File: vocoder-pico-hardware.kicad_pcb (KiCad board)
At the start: 2 copper layers, 57 x 108 mm, 68 parts, among them J1 Conn_02x05_Odd_Even, J2 AudioJack2_SwitchT, J3 AudioJack2_SwitchT, Q1 BC547, Q2 BC547, Q3 BC547, Q4 BC547, SW1 SW_Push, SW2 SW_Push, U1 TL072, U2 LM7805_TO220, U3 PCM5100A, U4 SC39-11GWA, U5 SC39-11GWA, U6 SC39-11GWA, U7 SC39-11GWA, U8 MCP6002-xP

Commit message: re-route D3
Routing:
- net +5V: track 20.1 -> 107.5 mm
- net Vsys: track 0.00 -> 20.8 mm

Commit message: add vdd on potentiometers
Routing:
- net Vdd: track 163.3 -> 205.8 mm, vias 0 -> 1
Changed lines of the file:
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@@
+	)
+	(segment
+		(start 58.559 59.659)
+		(end 73.721 59.659)
+		(width 0.5)
+		(layer "F.Cu")
+		(net 20)
 	)
 	(segment
@@
 	)
 	(segment
+		(start 81.279 62.199)
+		(end 81.279 60.421108)
+		(width 0.5)
+		(layer "F.Cu")
+		(net 20)
+	)
+	(segment
 		(start 80.3625 75.075)
 		(end 77.425 75.075)
@@
 	)
 	(segment
+		(start 81.279 60.421108)
+		(end 82.041108 59.659)
+		(width 0.5)
+		(layer "F.Cu")
+		(net 20)
+	)
+	(segment
 		(start 70.485 73.98)
 		(end 70.485 71.815)
@@
 	)
 	(segment
+		(start 82.041108 59.659)
+		(end 83.158999 59.659)
+		(width 0.5)
+		(layer "F.Cu")
+		(net 20)
+	)
+	(segment
 		(start 77.243182 110.743182)
 		(end 77.5 111)
@@
 	)
 	(segment
+		(start 82.58 63.5)
+		(end 81.279 62.199)
+		(width 0.5)
+		(layer "F.Cu")
+		(net 20)
+	)
+	(segment
 		(start 80.3625 74.1375)
 		(end 80.3625 75.025)
@@
 	)
 	(segment
+		(start 83.158999 59.659)
+		(end 84.968962 61.468963)
+		(width 0.5)
+		(layer "F.Cu")
+		(net 20)
+	)
+	(segment
+		(start 73.721 59.659)
+		(end 75.5 61.438)
+		(width 0.5)
+		(layer "F.Cu")
+		(net 20)
+	)
+	(segment
 		(start 80.3625 77.025)
 		(end 81.475 77.025)
@@
 	)
 	(segment
+		(start 75.5 61.438)
+		(end 75.5 66)
+		(width 0.5)
+		(layer "F.Cu")
+		(net 20)
+	)
+	(segment
 		(start 67.354 98.043182)
 		(end 67.354 81.598)
@@
 	)
 	(segment
+		(start 56.9 58)
+		(end 58.559 59.659)
+		(width 0.5)
+		(layer "F.Cu")
+		(net 20)
+	)
+	(segment
 		(start 76.625 79.625)
 		(end 77.25 79)
@@
 		(net 20)
 	)
+	(via
+		(at 84.968962 61.468963)
+		(size 0.6)
+		(drill 0.3)
+		(layers "F.Cu" "B.Cu")
+		(net 20)
+	)
+	(segment
+		(start 89.631037 61.468963)
+		(end 93.1 58)
+		(width 0.5)
+		(layer "B.Cu")
+		(net 20)
+	)
+	(segment
+		(start 84.968962 61.468963)
+		(end 89.631037 61.468963)
+		(width 0.5)
+		(layer "B.Cu")
+		(net 20)
+	)

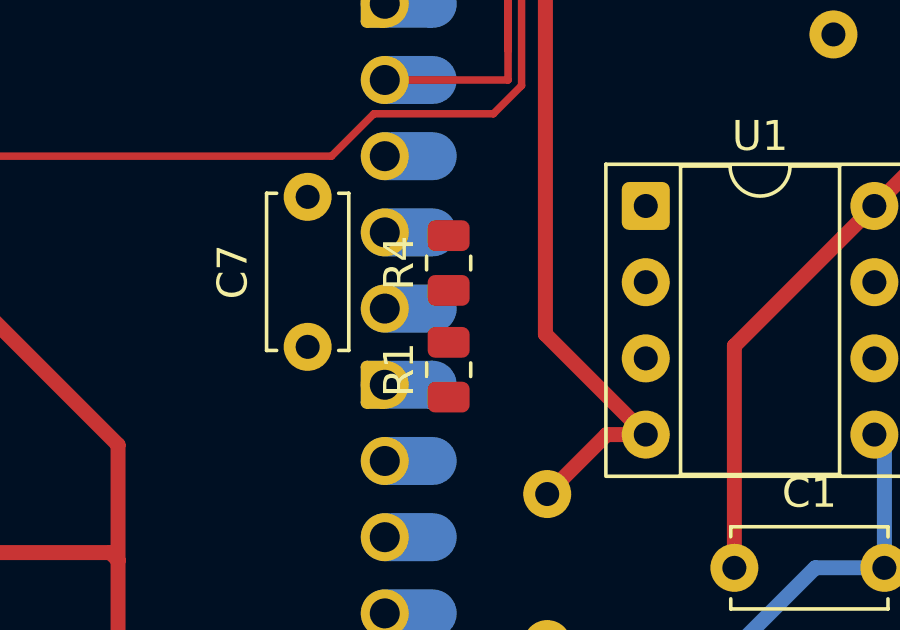
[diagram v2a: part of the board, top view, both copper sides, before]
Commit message: repossitioning smd resistors
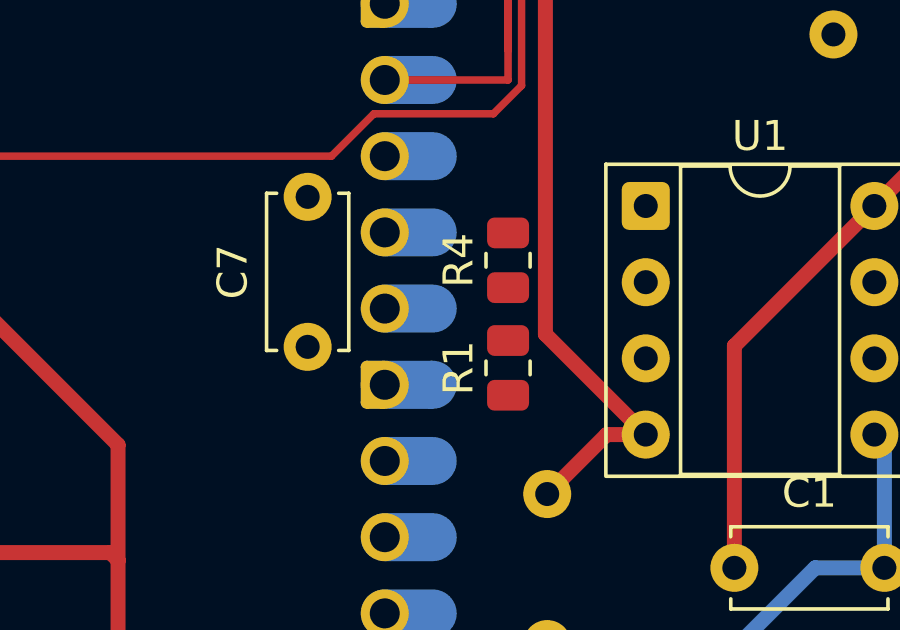
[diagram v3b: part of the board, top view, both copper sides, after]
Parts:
- moved R4 1.98 mm to (90.5, 101.0)
- moved R1 1.98 mm to (90.5, 104.6)
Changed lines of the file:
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@@
 	(footprint "Resistor_SMD:R_0805_2012Metric"
 		(layer "F.Cu")
-		(at 88.519 101.092 90)
+		(at 90.5 101 90)
 		(descr "Resistor SMD 0805 (2012 Metric), square (rectangular) end terminal, IPC-7351 nominal, (Body size source: IPC-SM-782 page 72, https://www.pcb-3d.com/wordpress/wp-content/uploads/ipc-sm-782a_amendment_1_and_2.pdf), generated with kicad-footprint-generator")
 		(tags "resistor")
@@
 	(footprint "Resistor_SMD:R_0805_2012Metric"
 		(layer "F.Cu")
-		(at 88.519 104.648 90)
+		(at 90.5 104.5875 90)
 		(descr "Resistor SMD 0805 (2012 Metric), square (rectangular) end terminal, IPC-7351 nominal, (Body size source: IPC-SM-782 page 72, https://www.pcb-3d.com/wordpress/wp-content/uploads/ipc-sm-782a_amendment_1_and_2.pdf), generated with kicad-footprint-generator")
 		(tags "resistor")

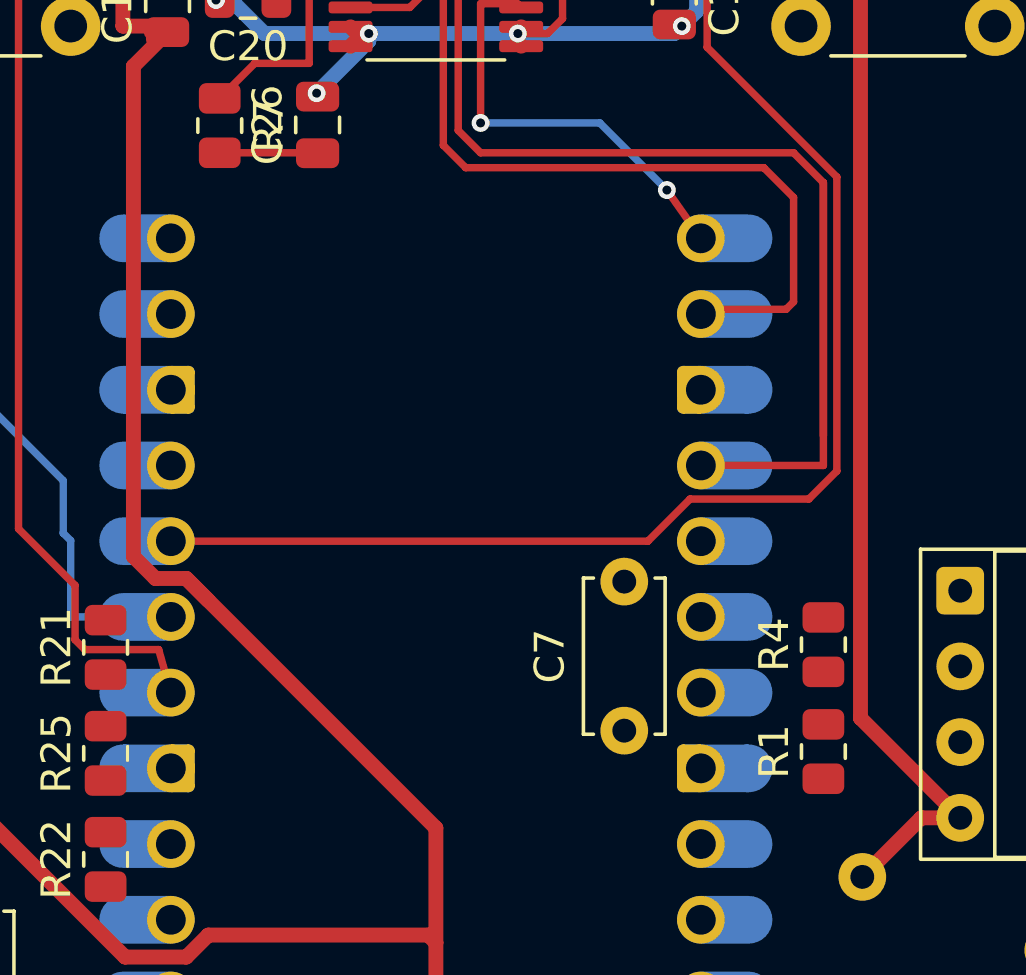
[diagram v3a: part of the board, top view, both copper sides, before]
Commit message: fix warnings (dangling tracks)
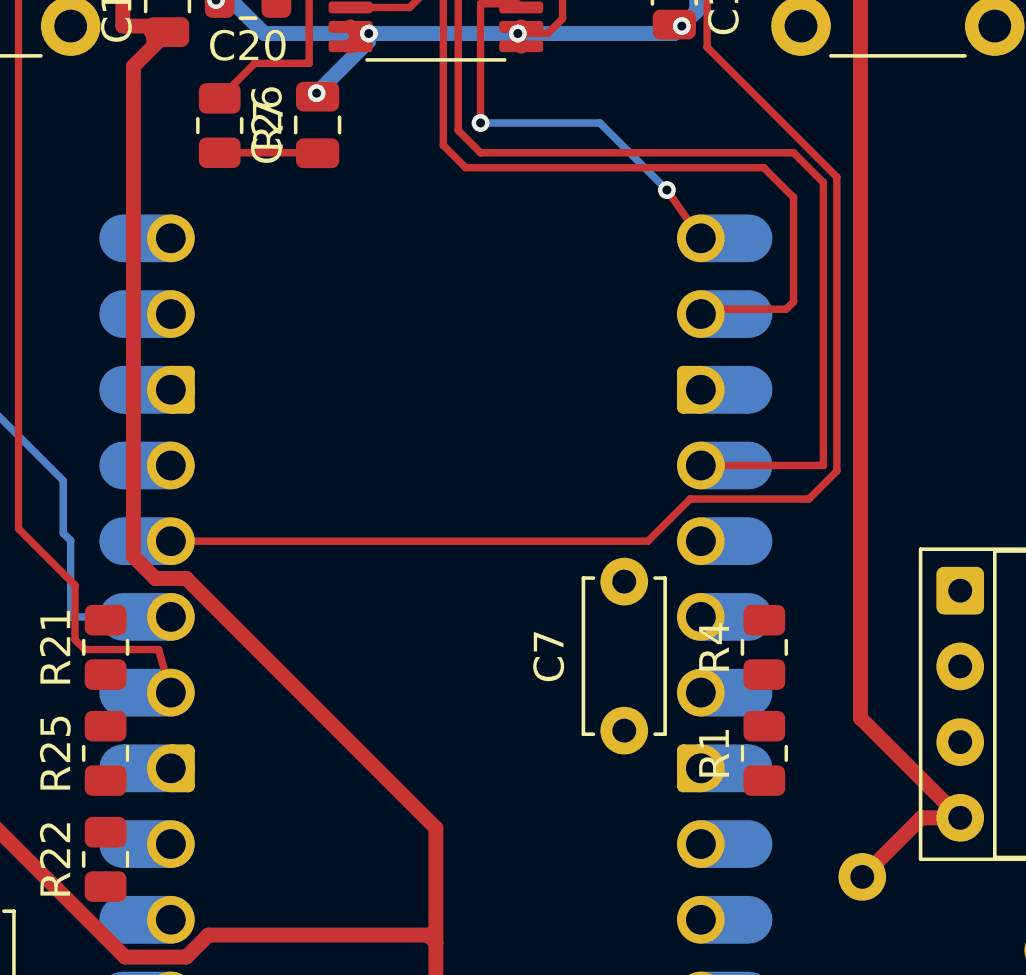
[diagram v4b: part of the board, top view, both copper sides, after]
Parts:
- moved R4 1.98 mm to (88.5, 101.1)
- moved R1 1.98 mm to (88.5, 104.6)
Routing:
- net Net-(A1-GPIO18): track 41.9 -> 33.4 mm
- net Vdd: track 205.8 -> 204.7 mm

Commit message: rename u1 => u8, u8 => u1
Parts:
- renumbered U8 to U1, U1 to U8
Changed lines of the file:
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@@
 	(net 59 "Net-(U3-LDOO)")
 	(net 60 "Net-(U3-VNEG)")
-	(net 61 "Net-(U8A-+)")
-	(net 62 "Net-(U8A--)")
+	(net 61 "Net-(U1A-+)")
+	(net 62 "Net-(U1A--)")
 	(net 63 "Net-(C11-Pad2)")
-	(net 64 "Net-(U8B--)")
-	(net 65 "Net-(U1A--)")
-	(net 66 "Net-(U1B--)")
+	(net 64 "Net-(U1B--)")
+	(net 65 "Net-(U8A--)")
+	(net 66 "Net-(U8B--)")
 	(net 67 "Net-(C7-Pad2)")
 	(net 68 "unconnected-(J3-PadTN)")
@@
 			(layers "F.Cu" "F.Mask" "F.Paste")
 			(roundrect_rratio 0.243902)
-			(net 65 "Net-(U1A--)")
+			(net 65 "Net-(U8A--)")
 			(pintype "passive")
 		)
@@
 		(descr "8-lead though-hole mounted DIP package, row spacing 7.62mm (300 mils), Socket")
 		(tags "THT DIP DIL PDIP 2.54mm 7.62mm 300mil Socket")
-		(property "Reference" "U1"
+		(property "Reference" "U8"
 			(at 3.81 -2.33 0)
 			(layer "F.SilkS")
@@
 			(layers "*.Cu" "*.Mask")
 			(remove_unused_layers no)
-			(net 65 "Net-(U1A--)")
+			(net 65 "Net-(U8A--)")
 			(pinfunction "-")
 			(pintype "input")
@@
 			(layers "*.Cu" "*.Mask")
 			(remove_unused_layers no)
-			(net 66 "Net-(U1B--)")
+			(net 66 "Net-(U8B--)")
 			(pinfunction "-")
 			(pintype "input")
@@
 			(layers "*.Cu" "*.Mask")
 			(remove_unused_layers no)
-			(net 66 "Net-(U1B--)")
+			(net 66 "Net-(U8B--)")
 			(pintype "output")
 		)
@@
 			(layers "F.Cu" "F.Mask" "F.Paste")
 			(roundrect_rratio 0.243902)
-			(net 61 "Net-(U8A-+)")
+			(net 61 "Net-(U1A-+)")
 			(pintype "passive")
 		)
@@
 			(layers "F.Cu" "F.Mask" "F.Paste")
 			(roundrect_rratio 0.243902)
-			(net 65 "Net-(U1A--)")
+			(net 65 "Net-(U8A--)")
 			(pintype "passive")
 		)
@@
 			(layers "*.Cu" "*.Mask")
 			(remove_unused_layers no)
-			(net 62 "Net-(U8A--)")
+			(net 62 "Net-(U1A--)")
 			(pintype "passive")
 		)
@@
 			(layers "F.Cu" "F.Mask" "F.Paste")
 			(roundrect_rratio 0.243902)
-			(net 61 "Net-(U8A-+)")
+			(net 61 "Net-(U1A-+)")
 			(pintype "passive")
 		)
@@
 			(layers "*.Cu" "*.Mask")
 			(remove_unused_layers no)
-			(net 61 "Net-(U8A-+)")
+			(net 61 "Net-(U1A-+)")
 			(pintype "passive")
 		)
@@
 		(descr "8-lead though-hole mounted DIP package, row spacing 7.62mm (300 mils), Socket")
 		(tags "THT DIP DIL PDIP 2.54mm 7.62mm 300mil Socket")
-		(property "Reference" "U8"
+		(property "Reference" "U1"
 			(at 3.81 -2.33 0)
 			(layer "F.SilkS")
@@
 			(layers "*.Cu" "*.Mask")
 			(remove_unused_layers no)
-			(net 62 "Net-(U8A--)")
+			(net 62 "Net-(U1A--)")
 			(pinfunction "-")
 			(pintype "input")
@@
 			(layers "*.Cu" "*.Mask")
 			(remove_unused_layers no)
-			(net 61 "Net-(U8A-+)")
+			(net 61 "Net-(U1A-+)")
 			(pinfunction "+")
 			(pintype "input")
@@
 			(layers "*.Cu" "*.Mask")
 			(remove_unused_layers no)
-			(net 61 "Net-(U8A-+)")
+			(net 61 "Net-(U1A-+)")
 			(pinfunction "+")
 			(pintype "input")
@@
 			(layers "*.Cu" "*.Mask")
 			(remove_unused_layers no)
-			(net 64 "Net-(U8B--)")
+			(net 64 "Net-(U1B--)")
 			(pinfunction "-")
 			(pintype "input")
@@
 			(layers "*.Cu" "*.Mask")
 			(remove_unused_layers no)
-			(net 64 "Net-(U8B--)")
+			(net 64 "Net-(U1B--)")
 			(pintype "output")
 		)
@@
 			(layers "F.Cu" "F.Mask" "F.Paste")
 			(roundrect_rratio 0.243902)
-			(net 62 "Net-(U8A--)")
+			(net 62 "Net-(U1A--)")
 			(pintype "passive")
 		)
@@
 			(layers "*.Cu" "*.Mask")
 			(remove_unused_layers no)
-			(net 65 "Net-(U1A--)")
+			(net 65 "Net-(U8A--)")
 			(pintype "passive")
 		)
@@
 			(layers "F.Cu" "F.Mask" "F.Paste")
 			(roundrect_rratio 0.243902)
-			(net 62 "Net-(U8A--)")
+			(net 62 "Net-(U1A--)")
 			(pintype "passive")
 		)

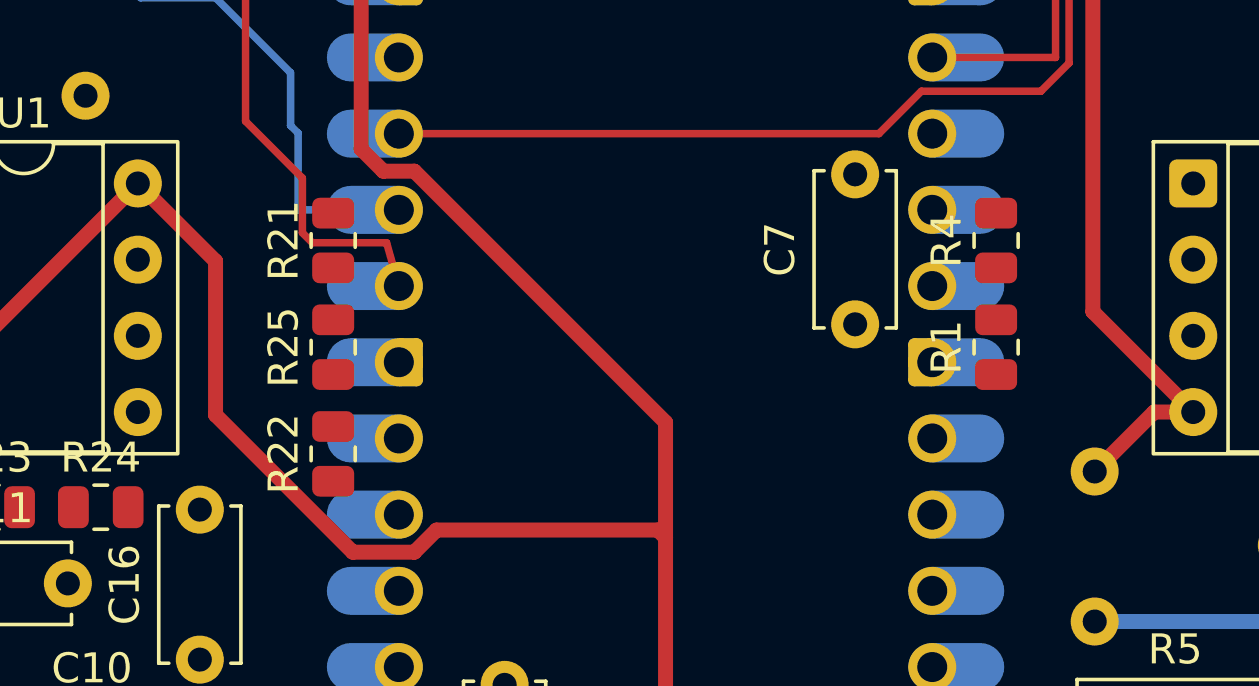
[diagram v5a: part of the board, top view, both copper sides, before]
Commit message: repositioning smd resistors
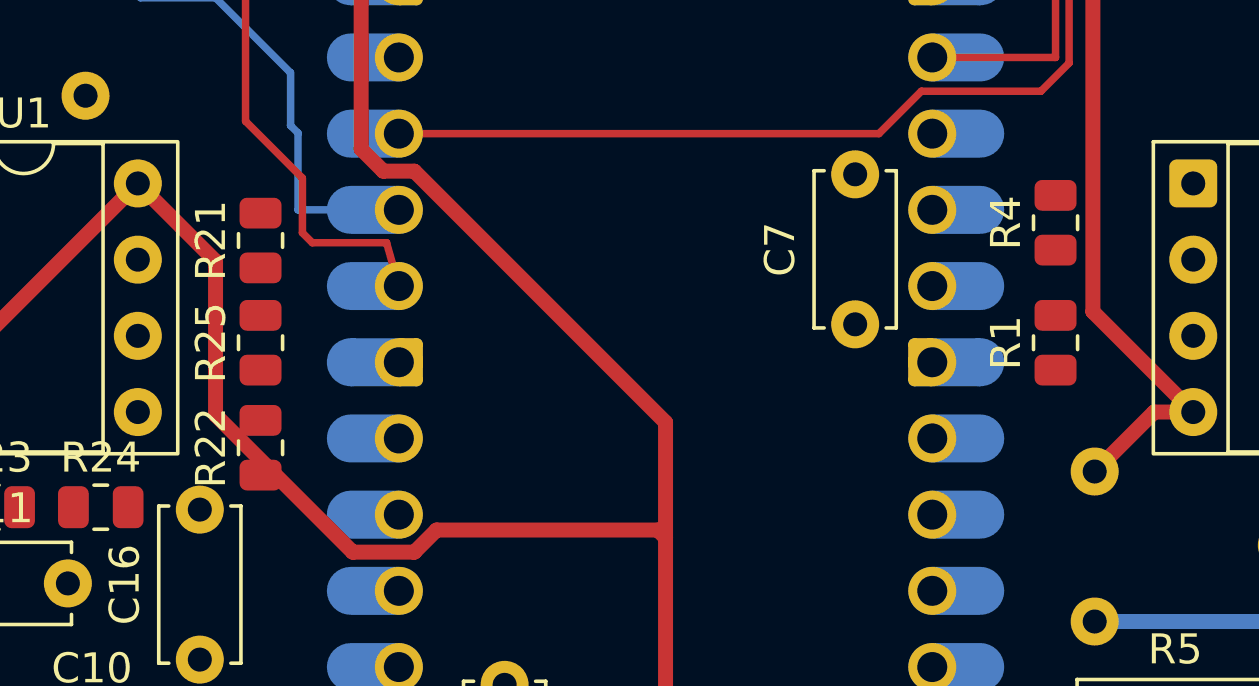
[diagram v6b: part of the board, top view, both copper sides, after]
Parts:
- moved R22 2.43 mm to (64.0, 108.0)
- moved R25 2.43 mm to (64.0, 104.5)
- moved R21 2.42 mm to (64.0, 101.1)
- moved R4 2.07 mm to (90.5, 100.5)
- moved R1 1.99 mm to (90.5, 104.5)

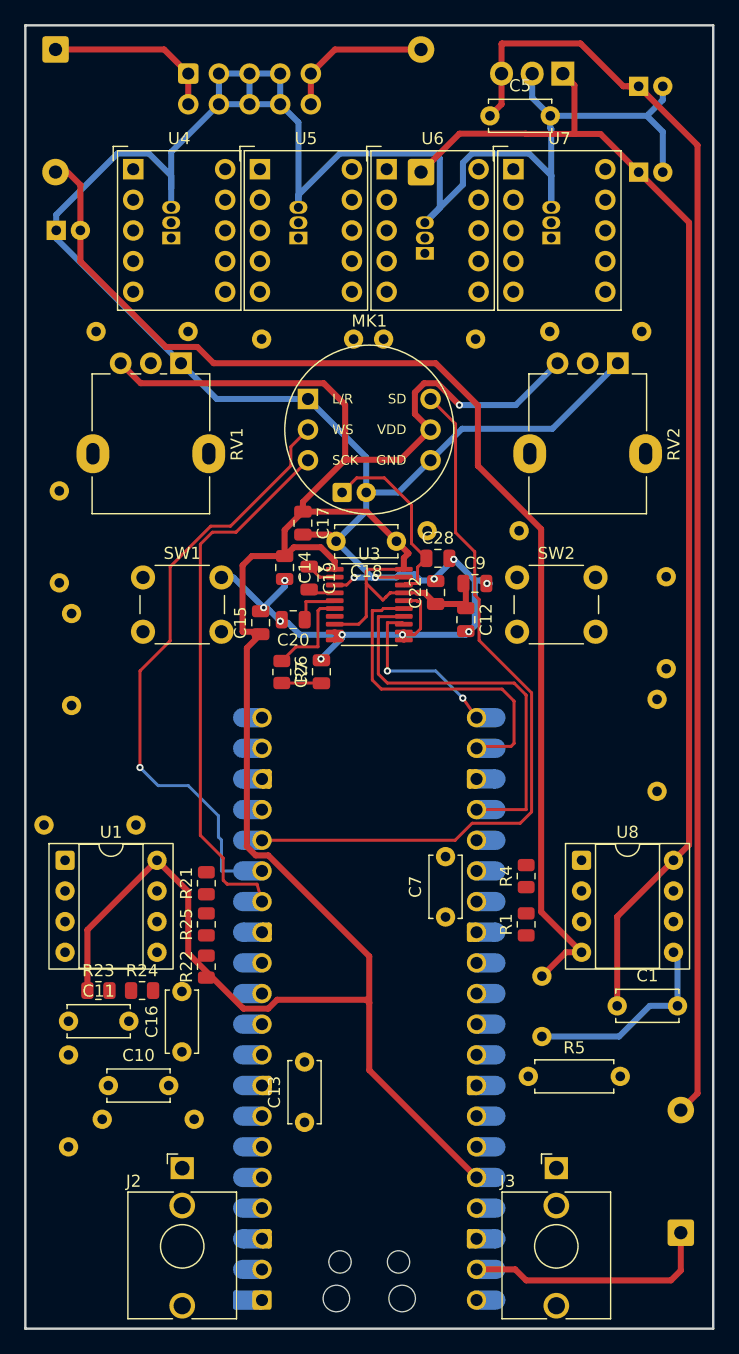
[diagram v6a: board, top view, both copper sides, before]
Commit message: repositioning components
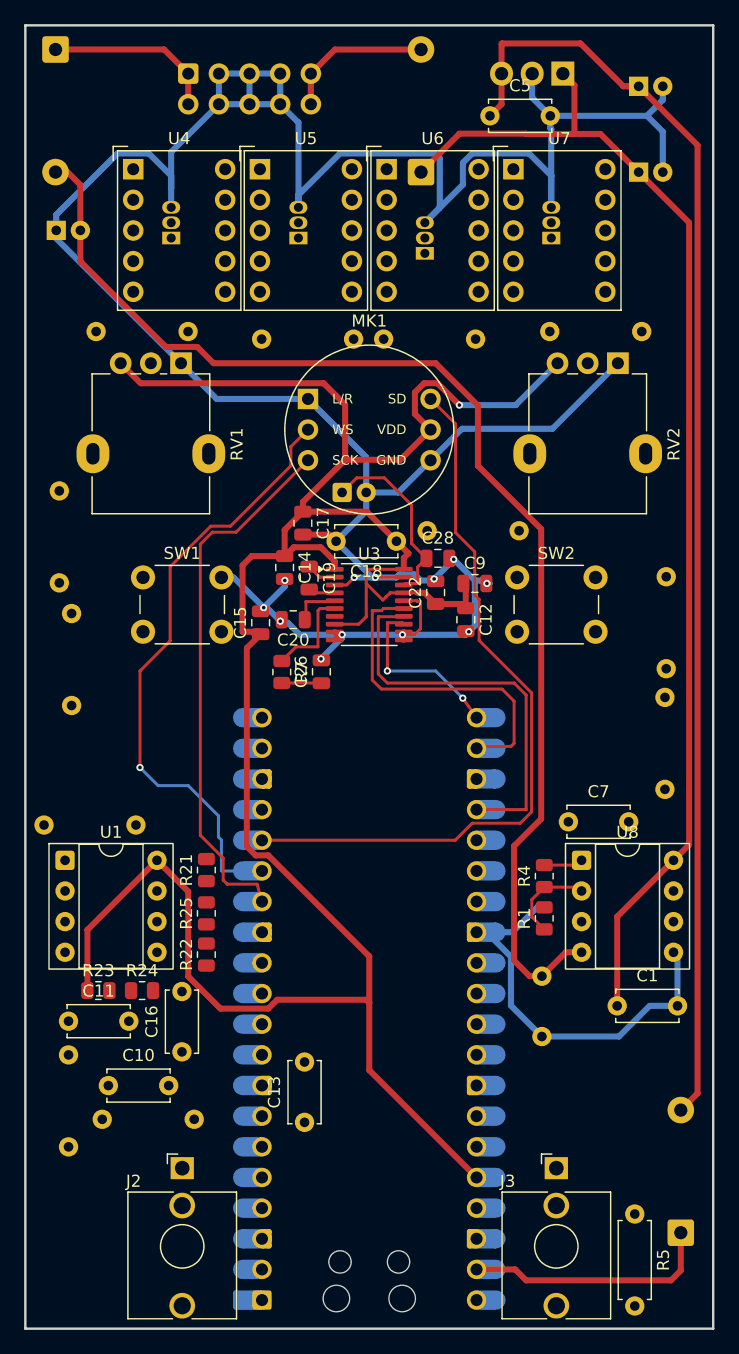
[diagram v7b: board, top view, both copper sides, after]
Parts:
- moved R5 14.4 mm to (99.5, 128.5), turned to -90 degrees
- moved C7 12.9 mm to (94.0, 96.0), turned to 0 degrees
- moved R1 1.58 mm to (92.0, 104.0)
- moved R4 1.50 mm to (92.0, 100.5)
- moved R21 1.09 mm to (64.0, 100.0)
- moved R22 1.00 mm to (64.0, 107.0)
- moved R25 0.91 mm to (64.0, 103.6)
- moved R17 0.67 mm to (102.0, 93.3)
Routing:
- net GND: track 267.0 -> 283.3 mm
- net Net-(U8A--): track 0.00 -> 7.57 mm
- net Net-(C7-Pad2): track 0.00 -> 3.25 mm
- net -12V: track 98.7 -> 101.8 mm
- net Vdd: track 204.7 -> 205.9 mm

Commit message: continue routing the output section
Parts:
- moved C7 5.52 mm to (99.5, 95.5), turned to 180 degrees
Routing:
- net OUtL: track 3.29 -> 48.7 mm, vias 0 -> 2
- net Net-(C7-Pad2): track 3.25 -> 38.8 mm, vias 0 -> 1
- net GND: track 283.3 -> 304.2 mm
- net Net-(U8A--): track 7.57 -> 18.0 mm
- net Net-(J3-PadT): track 0.00 -> 6.51 mm
- net -12V: track 101.8 -> 106.4 mm, vias 0 -> 1
